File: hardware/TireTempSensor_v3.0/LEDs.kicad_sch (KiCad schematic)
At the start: 10 parts

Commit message: Propozycja layoutu na spotkanie
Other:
- note added: "Potrzebne???"
- moved on the sheet: D3, D4, D5, R7, R8, R9

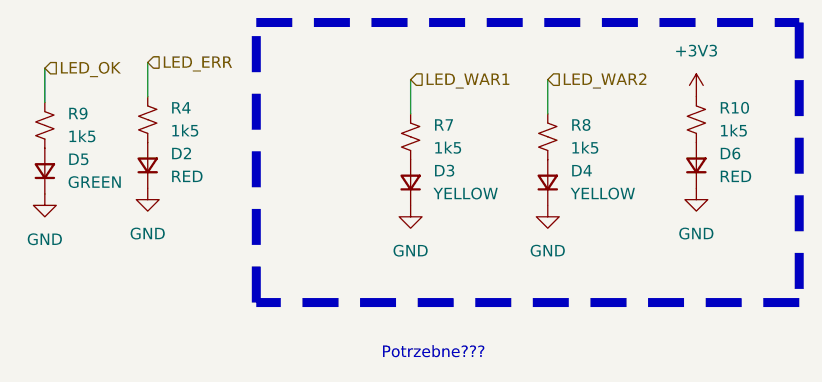
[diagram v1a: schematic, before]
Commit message: Nowy layout, nowe tvsy
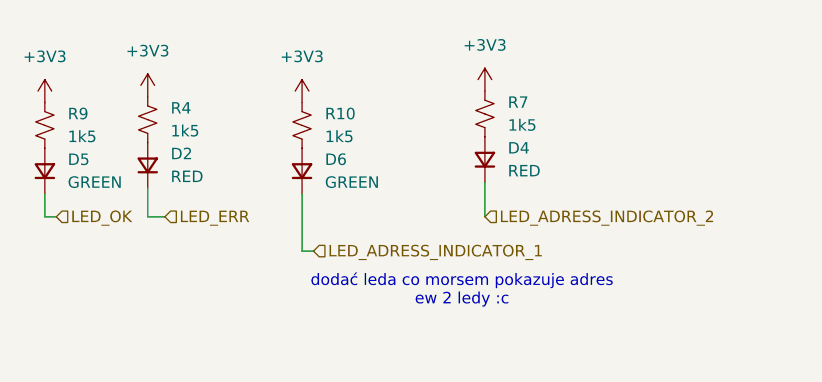
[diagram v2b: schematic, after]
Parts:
- removed D3: YELLOW, Diode_SMD:D_0603_1608Metric, symbol Device:D_Small
- removed R8: 1k5, Resistor_SMD:R_0603_1608Metric, symbol Device:R_Small_US
- D4: value YELLOW -> RED
- D6: value RED -> GREEN
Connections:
- net LED_WAR1 is gone; now on net +3V3: R7.1
- net +3V3: now also R4.1, R9.1
- net LED_ERR: now also D2.1 (K); no longer R4.1
- net LED_OK: now also D5.1 (K); no longer R9.1
- net at R7.2: now also D4.2 (A)
- removed net GND: D2.1 (K), D4.1 (K), D5.1 (K), D6.1 (K)
- new net LED_ADRESS_INDICATOR_1: D6.1 (K)
- new net LED_ADRESS_INDICATOR_2: D4.1 (K)
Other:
- note added: "dodać leda co morsem pokazuje adres ew 2 ledy :c"
- note removed: "Potrzebne???"
